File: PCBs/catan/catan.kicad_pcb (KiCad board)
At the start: 2 copper layers, 110 x 95.3 mm, 65 parts, among them J1 Conn_01x04_Female, J2 Conn_01x06_Male, SW1 SW_MEC_5E, SW10 SW_MEC_5E, SW11 SW_MEC_5E, SW2 SW_MEC_5E, SW3 SW_MEC_5E, SW4 SW_MEC_5E, SW5 SW_MEC_5E, SW6 SW_MEC_5E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

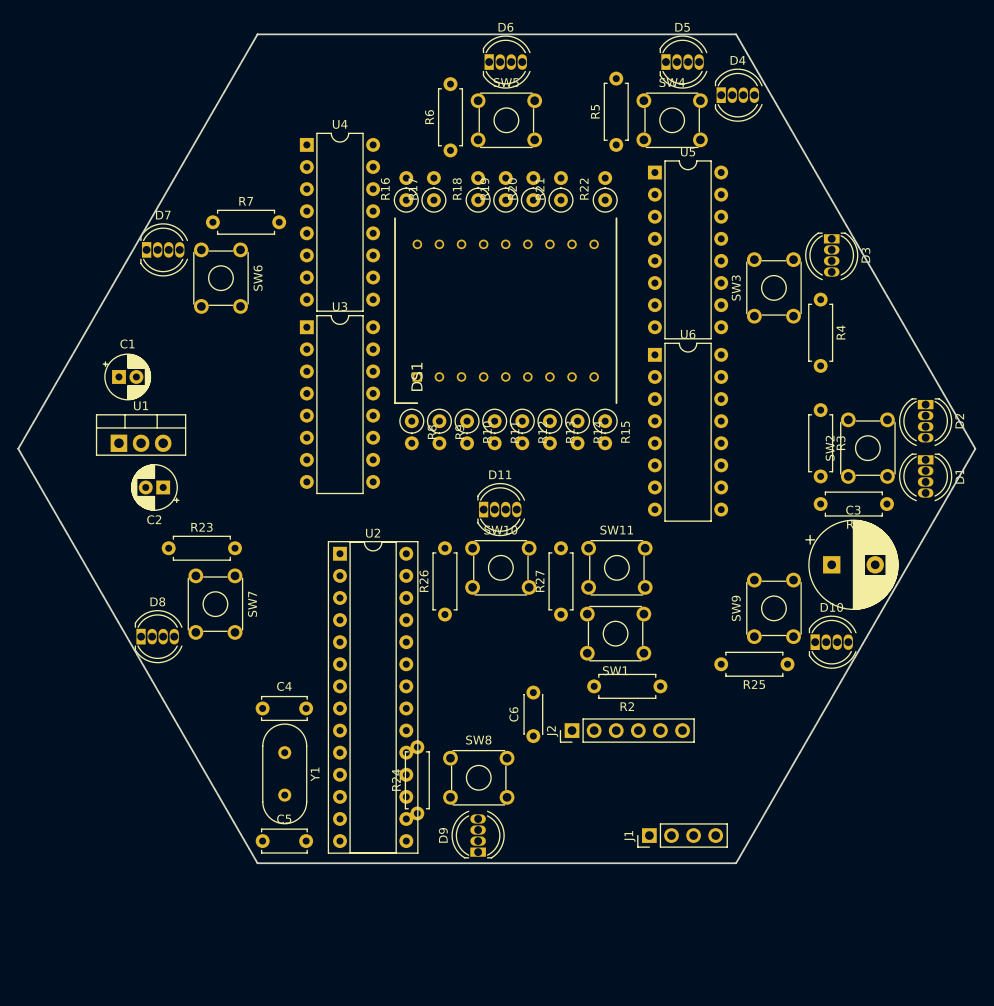
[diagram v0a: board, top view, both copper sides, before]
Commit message: flip display and interface components to back
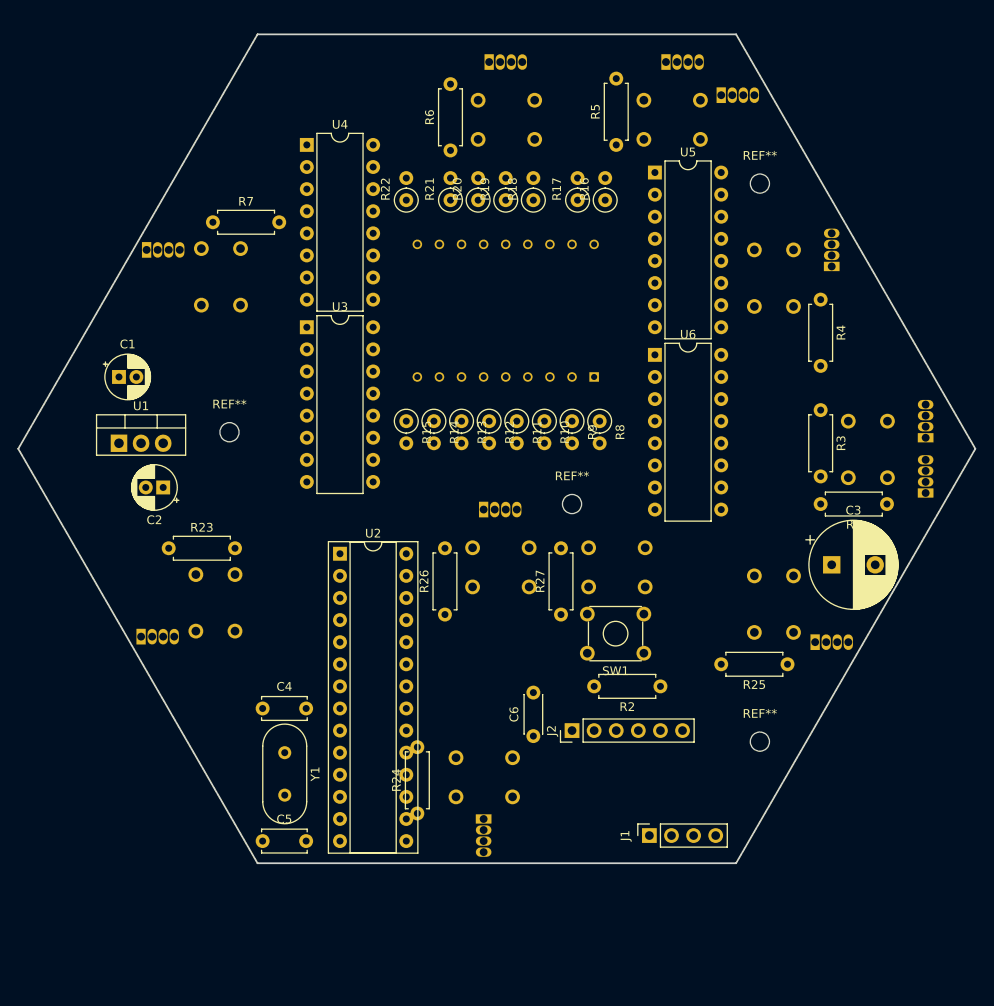
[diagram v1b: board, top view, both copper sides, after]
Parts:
- added REF**: MountingHole_2.2mm_M2, MountingHole:MountingHole_2.2mm_M2, F.Cu at (156.8, 116.8)
- added REF**: MountingHole_2.2mm_M2, MountingHole:MountingHole_2.2mm_M2, F.Cu at (156.8, 52.7)
- added REF**: MountingHole_2.2mm_M2, MountingHole:MountingHole_2.2mm_M2, F.Cu at (95.9, 81.3)
- added REF**: MountingHole_2.2mm_M2, MountingHole:MountingHole_2.2mm_M2, F.Cu at (135.3, 89.5)
- D1, D10, D11, D2, D3, D4, D5, D6, D7, D8, D9, DS1, SW10, SW11, SW2, SW3, SW4, SW5, SW6, SW7, SW8, SW9: moved to B.Cu
- J1: footprint Connector_PinHeader_2.54mm:PinHeader_1x04_P2.54mm_Vertical -> Connector_PinSocket_2.54mm:PinSocket_1x04_P2.54mm_Vertical
- moved R15 22.9 mm to (116.2, 80.0)
- moved R16 22.9 mm to (139.1, 54.6)
- moved R22 22.9 mm to (116.2, 54.6)
- moved R8 21.6 mm to (138.4, 80.0)
- moved DS1 20.3 mm to (137.8, 74.9)
- moved R14 16.5 mm to (119.4, 80.0)
- moved R17 16.5 mm to (135.9, 54.6)
- moved R9 15.2 mm to (135.3, 80.0)
- moved R21 12.7 mm to (121.3, 54.6)
- moved R13 10.2 mm to (122.6, 80.0)
- moved R10 8.89 mm to (132.1, 80.0)
- moved SW3 7.62 mm to (156.2, 60.3), turned to 270 degrees
- moved SW9 6.98 mm to (156.2, 97.8), turned to 270 degrees
- moved R18 6.35 mm to (130.8, 54.6)
- moved R20 6.35 mm to (124.5, 54.6)
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
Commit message: traces for rgb array
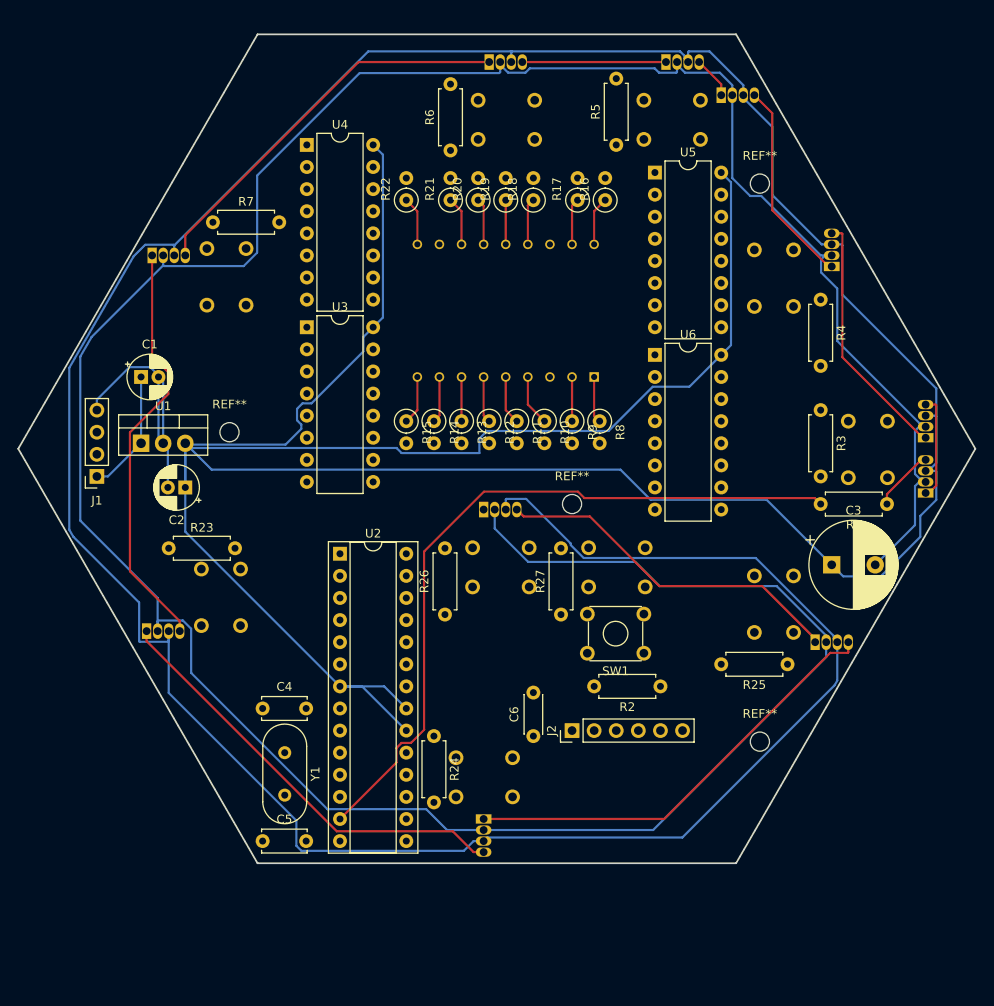
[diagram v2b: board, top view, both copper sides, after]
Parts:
- moved J1 75.7 mm to (80.6, 86.4), turned to 180 degrees
- moved R24 9.09 mm to (119.4, 116.2), turned to 270 degrees
- moved C2 2.54 mm to (90.8, 87.6)
- moved C1 2.54 mm to (85.7, 74.9)
- moved U1 2.54 mm to (85.7, 82.5)
- moved D8 0.90 mm to (86.4, 104.1)
- moved SW7 0.90 mm to (97.2, 103.5)
- moved D7 0.90 mm to (87.0, 61.0)
- moved SW6 0.64 mm to (97.8, 66.7)
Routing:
- net Net-(C2-Pad1): track 0.00 -> 652.4 mm
- net GND: track 0.00 -> 386.3 mm
- net Net-(R1-Pad2): track 0.00 -> 84.4 mm
- net Net-(D10-Pad4): track 0.00 -> 51.0 mm
- net Net-(D8-Pad1): track 0.00 -> 49.9 mm
- net Net-(D7-Pad1): track 0.00 -> 48.1 mm
- net Net-(D6-Pad1): track 0.00 -> 45.5 mm
- net Net-(D10-Pad1): track 0.00 -> 40.8 mm
- net Net-(D2-Pad1): track 0.00 -> 28.8 mm
- net Net-(D3-Pad1): track 0.00 -> 23.6 mm
- net Net-(D5-Pad1): track 0.00 -> 16.5 mm
- net +9V: track 0.00 -> 14.3 mm
- net Net-(D1-Pad1): track 0.00 -> 12.1 mm
- net Net-(D1-Pad4): track 0.00 -> 7.21 mm
- net Net-(DS1-Pad4): track 0.00 -> 5.87 mm
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
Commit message: fix button wiring
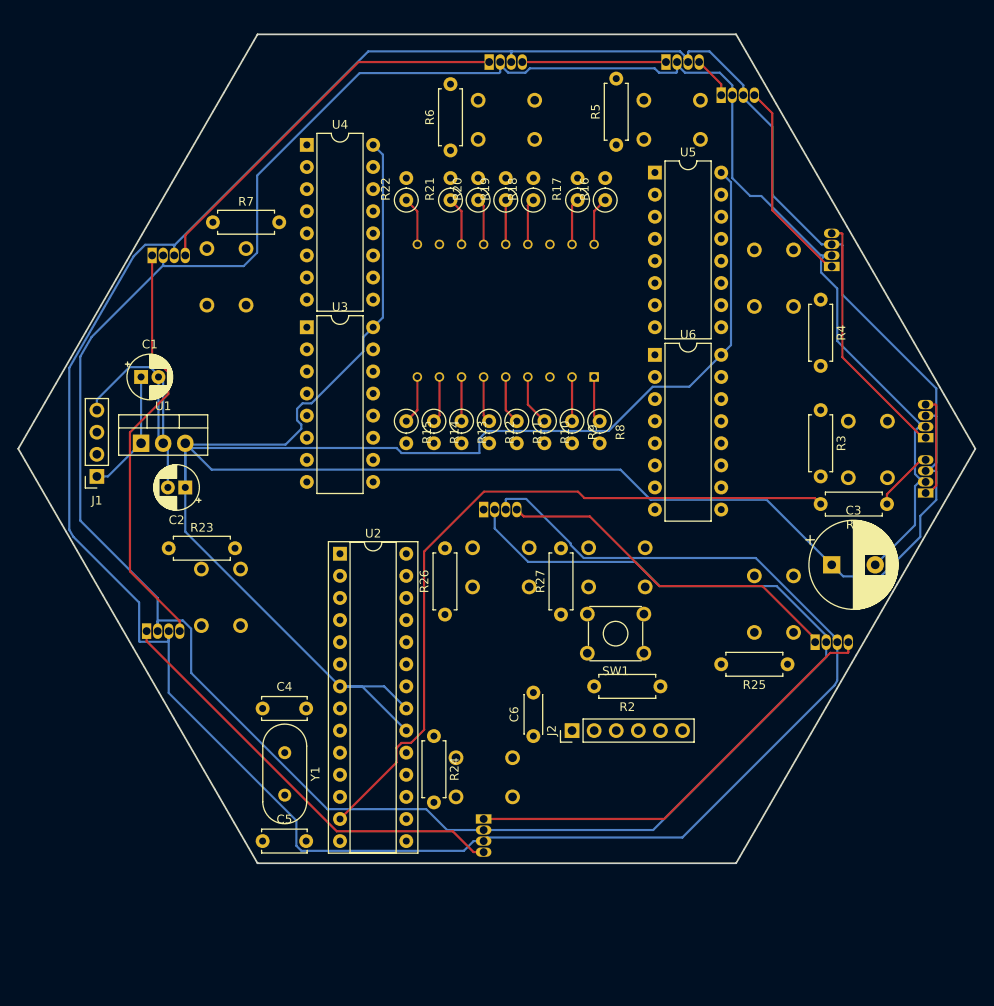
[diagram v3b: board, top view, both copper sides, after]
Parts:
- removed REF** (x4): MountingHole_2.2mm_M2, MountingHole:MountingHole_2.2mm_M2
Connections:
- D11 pad 1: Net-(D11-Pad1) -> (no net)
- DS1 pad 3: Net-(DS1-Pad3) -> (no net)
- J2 pad 5: Net-(J2-Pad5) -> (no net)
- SW1 pad 2: GND -> (no net)
- SW1 pad 3: Net-(SW1-Pad3) -> GND
- SW1 pad 4: Net-(SW1-Pad4) -> (no net)
- SW10 pad 2: Net-(C2-Pad1) -> (no net)
- SW10 pad 3: Net-(SW10-Pad3) -> Net-(C2-Pad1)
- SW10 pad 4: Net-(SW10-Pad4) -> (no net)
- SW11 pad 2: Net-(C2-Pad1) -> (no net)
- SW11 pad 3: Net-(SW11-Pad3) -> Net-(C2-Pad1)
- SW11 pad 4: Net-(SW11-Pad4) -> (no net)
- SW2 pad 2: Net-(C2-Pad1) -> (no net)
- SW2 pad 3: Net-(SW2-Pad3) -> Net-(C2-Pad1)
- SW2 pad 4: Net-(SW2-Pad4) -> (no net)
- SW3 pad 2: Net-(C2-Pad1) -> (no net)
- SW3 pad 3: Net-(SW3-Pad3) -> Net-(C2-Pad1)
- SW3 pad 4: Net-(SW3-Pad4) -> (no net)
- SW4 pad 2: Net-(C2-Pad1) -> (no net)
- SW4 pad 3: Net-(SW4-Pad3) -> Net-(C2-Pad1)
- SW4 pad 4: Net-(SW4-Pad4) -> (no net)
- SW5 pad 2: Net-(C2-Pad1) -> (no net)
- SW5 pad 3: Net-(SW5-Pad3) -> Net-(C2-Pad1)
- SW5 pad 4: Net-(SW5-Pad4) -> (no net)
- SW6 pad 2: Net-(C2-Pad1) -> (no net)
- SW6 pad 3: Net-(SW6-Pad3) -> Net-(C2-Pad1)
- SW6 pad 4: Net-(SW6-Pad4) -> (no net)
- SW7 pad 2: Net-(C2-Pad1) -> (no net)
- SW7 pad 3: Net-(SW7-Pad3) -> Net-(C2-Pad1)
- SW7 pad 4: Net-(SW7-Pad4) -> (no net)
- SW8 pad 2: Net-(C2-Pad1) -> (no net)
- SW8 pad 3: Net-(SW8-Pad3) -> Net-(C2-Pad1)
- SW8 pad 4: Net-(SW8-Pad4) -> (no net)
- SW9 pad 2: Net-(C2-Pad1) -> (no net)
- SW9 pad 3: Net-(SW9-Pad3) -> Net-(C2-Pad1)
- SW9 pad 4: Net-(SW9-Pad4) -> (no net)
- U2 pad 11: Net-(U2-Pad11) -> (no net)
- U2 pad 12: Net-(U2-Pad12) -> (no net)
- U2 pad 28: Net-(U2-Pad28) -> (no net)
- U2 pad 4: Net-(U2-Pad4) -> (no net)
- U2 pad 5: Net-(U2-Pad5) -> (no net)
- U2 pad 6: Net-(U2-Pad6) -> (no net)
- U3 pad 7: Net-(U3-Pad7) -> (no net)
- U4 pad 10: Net-(U4-Pad10) -> (no net)
- U4 pad 7: Net-(U4-Pad7) -> (no net)
- U5 pad 10: Net-(U5-Pad10) -> (no net)
- U5 pad 13: Net-(U5-Pad13) -> (no net)
- U6 pad 10: Net-(U6-Pad10) -> (no net)
- U6 pad 13: Net-(U6-Pad13) -> (no net)
- U6 pad 7: Net-(U6-Pad7) -> (no net)
- U6 pad 9: Net-(U6-Pad9) -> (no net)

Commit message: remove traces... and fix orientation
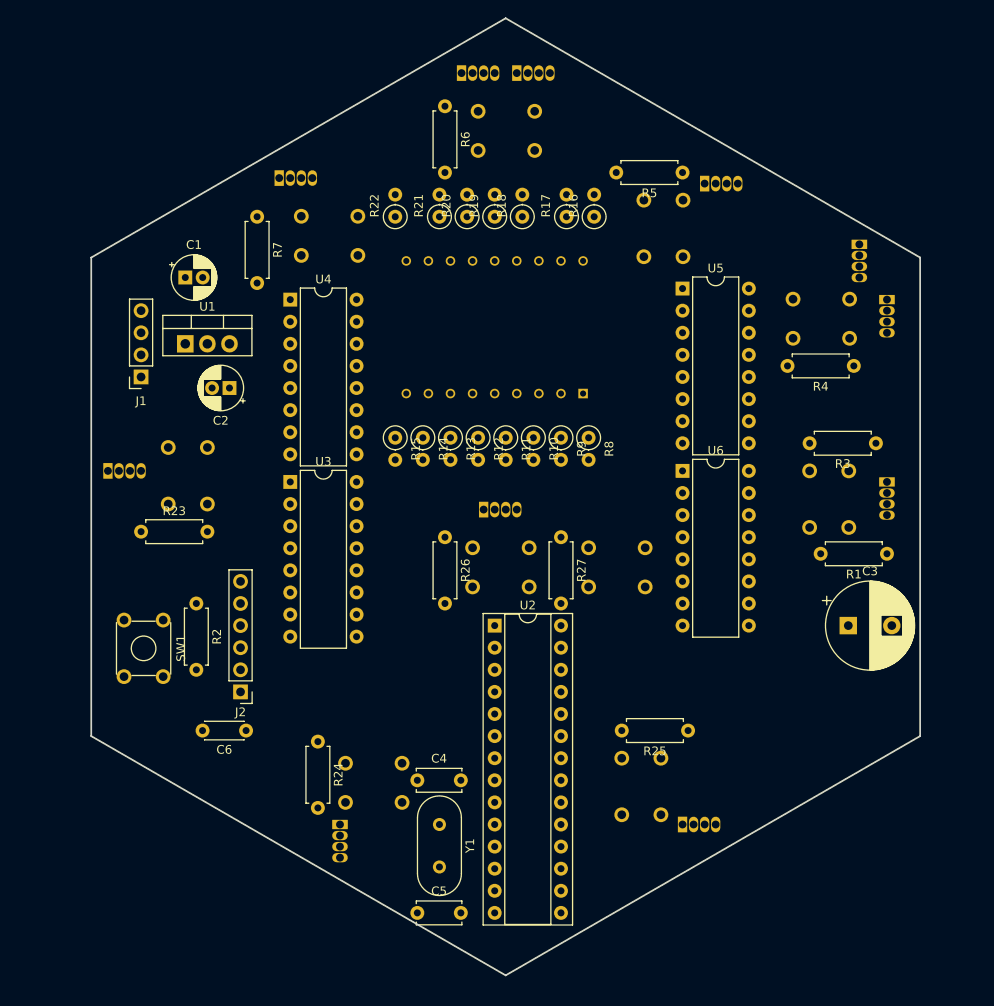
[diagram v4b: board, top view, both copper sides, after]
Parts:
- moved SW1 55.4 mm to (88.3, 102.9), turned to 270 degrees
- moved R2 54.2 mm to (92.1, 101.0), turned to 270 degrees
- moved J2 38.4 mm to (97.2, 111.1), turned to 180 degrees
- moved C6 33.0 mm to (97.8, 115.6), turned to 180 degrees
- moved SW9 25.9 mm to (141.0, 118.7)
- moved D10 25.9 mm to (148.0, 126.4)
- moved C4 19.6 mm to (117.5, 121.3)
- moved C5 19.6 mm to (117.5, 136.5)
- moved U2 19.6 mm to (126.4, 103.5)
- moved Y1 19.6 mm to (120.0, 126.4)
- moved D8 18.9 mm to (81.9, 85.7)
- moved U4 17.9 mm to (102.9, 66.0)
- moved U3 17.9 mm to (102.9, 87.0)
- moved D5 17.2 mm to (128.9, 40.0)
- moved D7 17.1 mm to (101.6, 52.1)
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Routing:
- net Net-(C2-Pad1): track 652.4 -> 0.00 mm
- net GND: track 386.3 -> 0.00 mm
- net Net-(R1-Pad2): track 84.4 -> 0.00 mm
- net Net-(D10-Pad4): track 51.0 -> 0.00 mm
- net Net-(D8-Pad1): track 49.9 -> 0.00 mm
- net Net-(D7-Pad1): track 48.1 -> 0.00 mm
- net Net-(D6-Pad1): track 45.5 -> 0.00 mm
- net Net-(D10-Pad1): track 40.8 -> 0.00 mm
- net Net-(D2-Pad1): track 28.8 -> 0.00 mm
- net Net-(D3-Pad1): track 23.6 -> 0.00 mm
- net Net-(D5-Pad1): track 16.5 -> 0.00 mm
- net +9V: track 14.3 -> 0.00 mm
- net Net-(D1-Pad1): track 12.1 -> 0.00 mm
- net Net-(D1-Pad4): track 7.21 -> 0.00 mm
- net Net-(DS1-Pad4): track 5.87 -> 0.00 mm
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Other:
- board size 110 x 95.3 mm -> 95.3 x 110 mm

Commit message: more precise placement of components
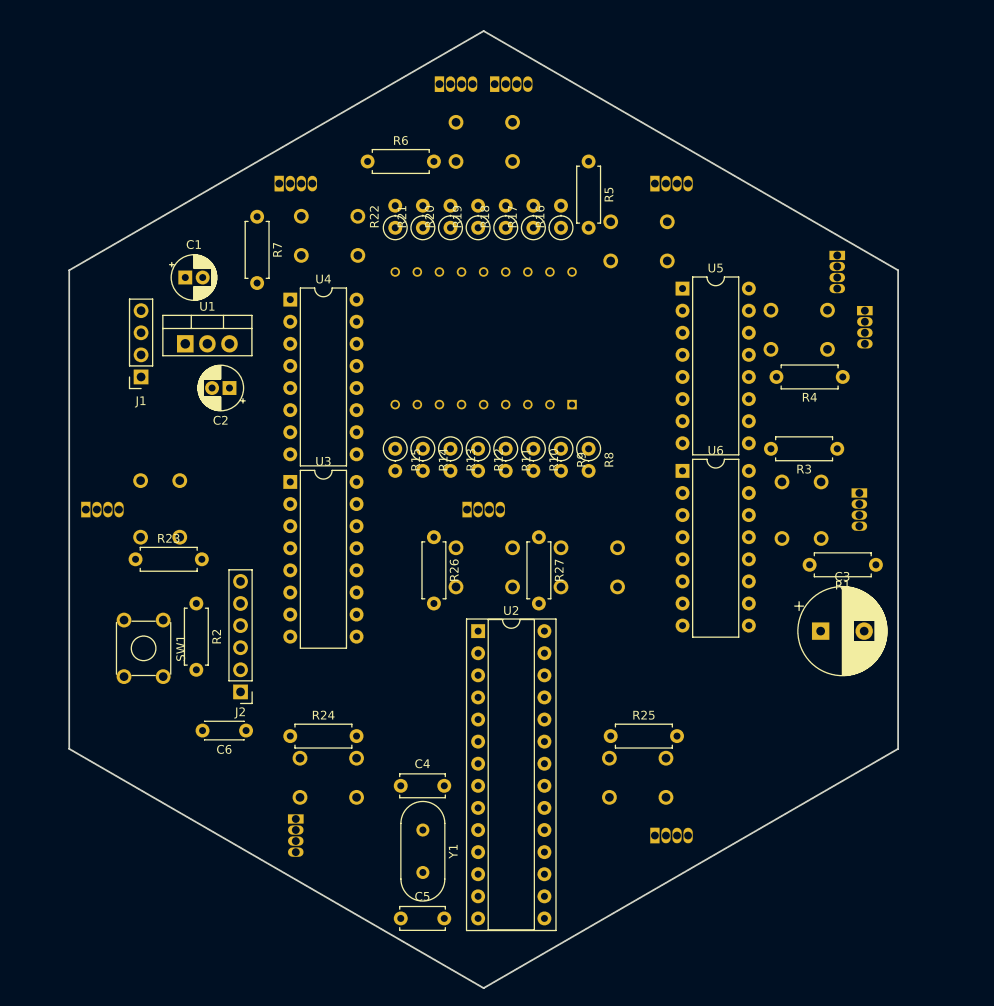
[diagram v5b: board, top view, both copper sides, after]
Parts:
- moved R6 10.9 mm to (111.8, 50.2), turned to 0 degrees
- moved R5 10.9 mm to (137.2, 50.2), turned to 270 degrees
- moved R25 8.91 mm to (139.7, 116.2), turned to 0 degrees
- moved SW4 7.96 mm to (139.7, 61.6), turned to 0 degrees
- moved D4 5.72 mm to (144.8, 52.7)
- moved SW8 5.24 mm to (110.5, 118.7), turned to 180 degrees
- moved D8 5.12 mm to (79.4, 90.2)
- moved D9 5.12 mm to (103.5, 125.7)
- moved SW9 5.08 mm to (146.1, 118.7), turned to 180 degrees
- moved SW7 4.96 mm to (90.2, 93.3)
- moved R3 4.49 mm to (165.7, 83.2)
- moved R17 4.02 mm to (130.8, 57.8)
- moved R16 4.02 mm to (134.0, 57.8)
- moved D10 3.42 mm to (144.8, 127.6)
- moved SW2 3.42 mm to (159.4, 87.0)
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
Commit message: power wiring buttons
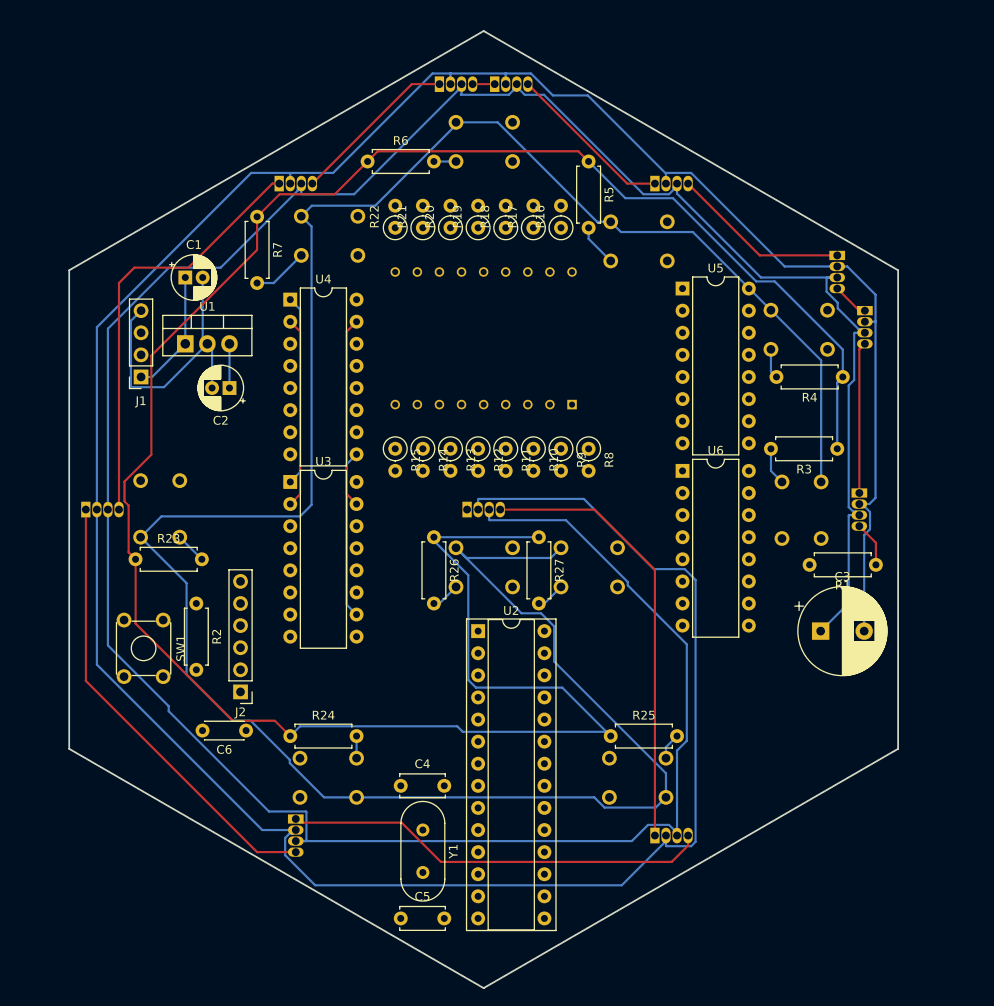
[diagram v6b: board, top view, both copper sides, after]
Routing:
- net GND: track 0.00 -> 633.6 mm
- net Net-(C2-Pad1): track 0.00 -> 611.8 mm
- net Net-(D8-Pad1): track 0.00 -> 52.0 mm
- net Net-(D10-Pad1): track 0.00 -> 51.2 mm
- net Net-(D7-Pad1): track 0.00 -> 49.2 mm
- net Net-(D10-Pad4): track 0.00 -> 49.1 mm
- net Net-(U2-Pad19): track 0.00 -> 21.9 mm
- net Net-(U2-Pad17): track 0.00 -> 21.9 mm
- net Net-(U2-Pad16): track 0.00 -> 21.9 mm
- net Net-(D3-Pad1): track 0.00 -> 20.6 mm
- net Net-(U3-Pad10): track 0.00 -> 19.3 mm
- net Net-(D6-Pad1): track 0.00 -> 19.3 mm
- net Net-(D4-Pad1): track 0.00 -> 19.3 mm
- net Net-(D1-Pad1): track 0.00 -> 17.4 mm
- net +9V: track 0.00 -> 14.3 mm
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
